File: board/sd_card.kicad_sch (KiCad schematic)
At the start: 1 part, among them J1301 MOLEX_5033981892

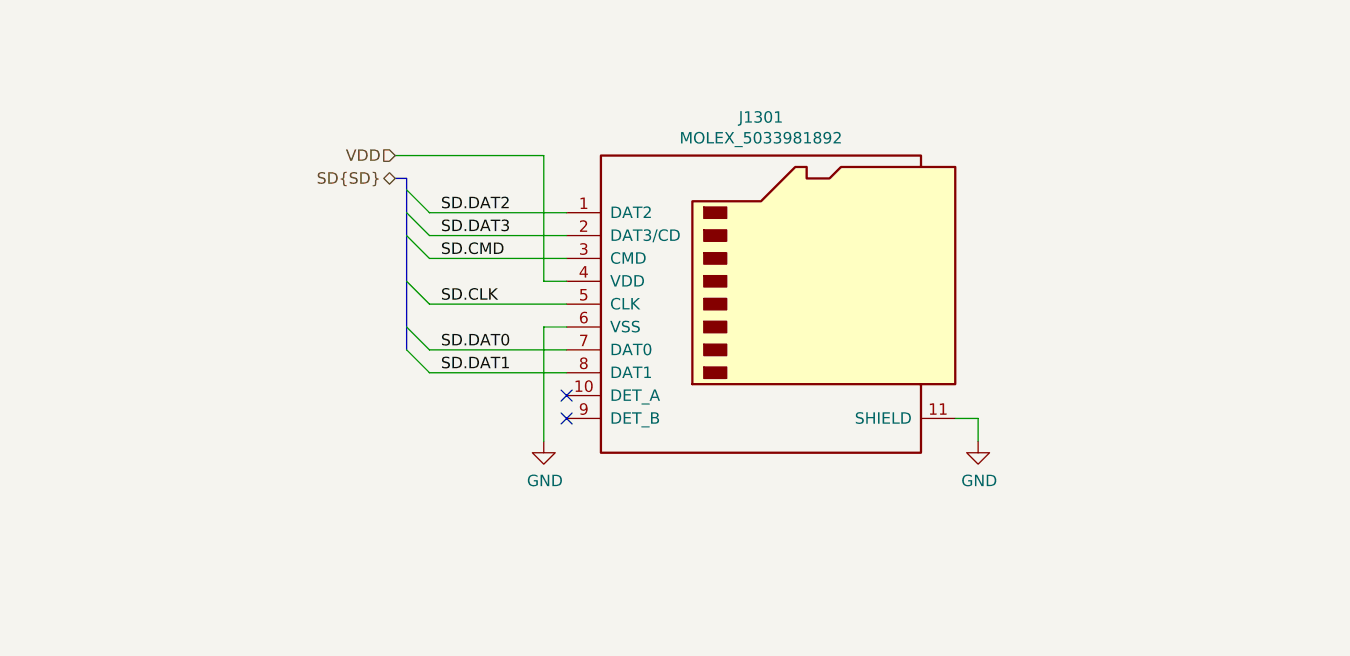
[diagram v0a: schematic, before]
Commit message: Added testpoints and other fixes
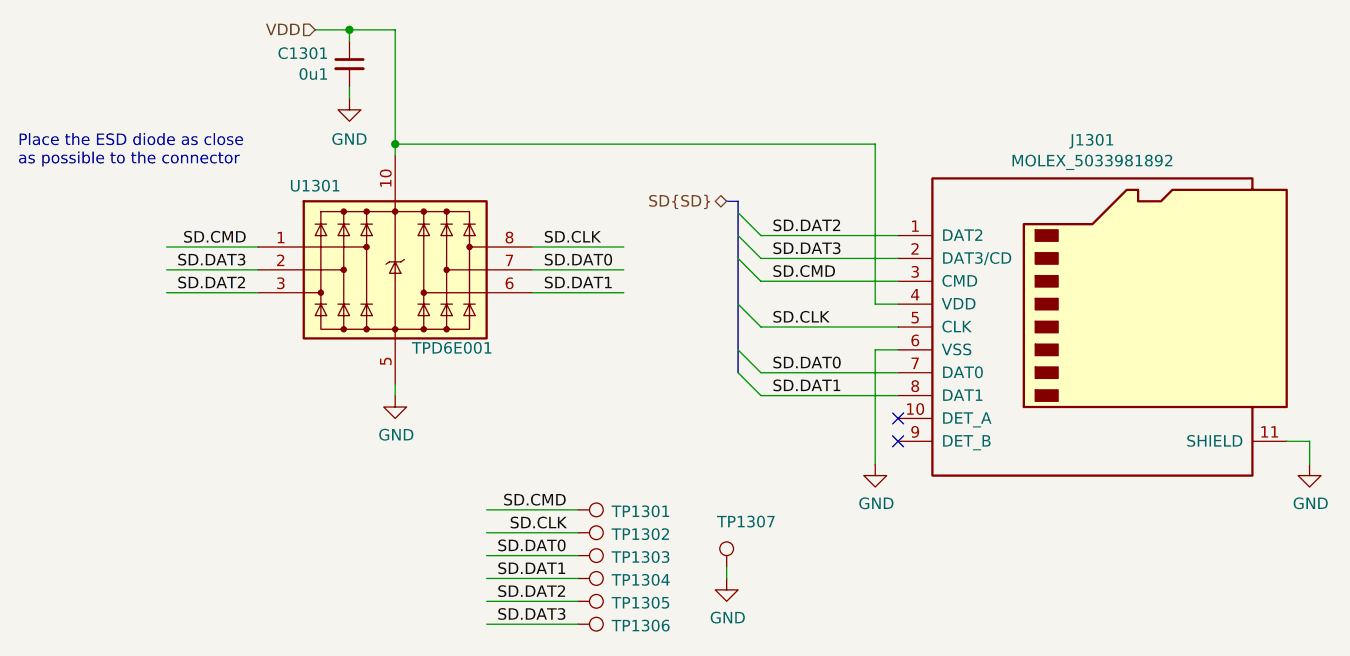
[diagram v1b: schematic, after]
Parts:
- added C1301: 0u1, DIYPie:C_0402_1005Metric, symbol Device:C_Small
- added TP1301, TP1302, TP1303, TP1304, TP1305, TP1306, TP1307: TestPoint, DIYPie:TestPoint_Pad_D1.5mm, symbol DIYPie:TestPoint
- added U1301: TPD6E001, DIYPie:TI_UQFN-10, symbol DIYPie:TPD6E001
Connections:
- net GND: now also C1301.2, TP1307.1, U1301.5
- net SD.CLK: now also TP1302.1, U1301.8
- net SD.CMD: now also TP1301.1, U1301.1
- net SD.DAT0: now also TP1303.1, U1301.7
- net SD.DAT1: now also TP1304.1, U1301.6
- net SD.DAT2: now also TP1305.1, U1301.3
- net SD.DAT3: now also TP1306.1, U1301.2
- net VDD: now also C1301.1, U1301.10
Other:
- note added: "Place the ESD diode as close as possible to the connector"
- moved on the sheet: J1301
